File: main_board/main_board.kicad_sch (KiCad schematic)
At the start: 17 parts

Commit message: fix(main_board): fix footprint
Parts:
- added R9: R, Resistor_SMD:R_0603_1608Metric_Pad0.98x0.95mm_HandSolder, symbol Device:R
- C1, C4: footprint (none) -> Capacitor_SMD:C_0603_1608Metric_Pad1.08x0.95mm_HandSolder
- C2, C3: footprint (none) -> Capacitor_SMD:C_0805_2012Metric_Pad1.18x1.45mm_HandSolder
- J1, J2: renamed from J?; footprint (none) -> Connector_Wuerth:Wuerth_WR-WTB_64800311622_1x03_P1.50mm_Vertical
- JSL1: footprint (none) -> Connector_PinHeader_2.00mm:PinHeader_1x08_P2.00mm_Vertical
- R1, R2, R3, R4, R5, R6, R7, R8: footprint (none) -> Resistor_SMD:R_0603_1608Metric_Pad0.98x0.95mm_HandSolder
- gave numbers to parts that had none: 2
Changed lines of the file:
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@@
 (kicad_sch (version 20230121) (generator eeschema)
   (paper "A4")
+  (symbol (lib_id "Device:R") (at 160.02 45.72 0) (unit 1)
+    (in_bom yes) (on_board yes) (dnp no) (fields_autoplaced)
+    (property "Reference" "R9" (at 162.56 44.45 0)
+      (effects (font (size 1.27 1.27)) (justify left))
+    )
+    (property "Value" "R" (at 162.56 46.99 0)
+      (effects (font (size 1.27 1.27)) (justify left))
+    )
+    (property "Footprint" "Resistor_SMD:R_0603_1608Metric_Pad0.98x0.95mm_HandSolder" (at 158.242 45.72 90)
+      (effects (font (size 1.27 1.27)) hide)
+    )
+    (property "Datasheet" "~" (at 160.02 45.72 0)
+      (effects (font (size 1.27 1.27)) hide)
+    )
+    (pin "1")
+    (pin "2")
+    (instances
+      (project "main_board"
+        (path "/e3ba9c21-8631-4c7f-8c4a-647134dd6657"
+          (reference "R9") (unit 1)
+        )
+      )
+    )
+  )
   (symbol (lib_id "Connector_Generic:Conn_01x03") (at 39.37 66.04 0) (unit 1)
     (in_bom yes) (on_board yes) (dnp no) (fields_autoplaced)
-    (property "Reference" "J?" (at 41.91 64.77 0)
+    (property "Reference" "J1" (at 41.91 64.77 0)
       (effects (font (size 1.27 1.27)) (justify left))
     )
@@
       (effects (font (size 1.27 1.27)) (justify left))
     )
-    (property "Footprint" "" (at 39.37 66.04 0)
+    (property "Footprint" "Connector_Wuerth:Wuerth_WR-WTB_64800311622_1x03_P1.50mm_Vertical" (at 39.37 66.04 0)
       (effects (font (size 1.27 1.27)) hide)
     )
@@
       (project "main_board"
         (path "/e3ba9c21-8631-4c7f-8c4a-647134dd6657"
-          (reference "J?") (unit 1)
+          (reference "J1") (unit 1)
         )
       )
@@
       (effects (font (size 1.27 1.27)) (justify left))
     )
-    (property "Footprint" "" (at 109.982 45.72 90)
+    (property "Footprint" "Resistor_SMD:R_0603_1608Metric_Pad0.98x0.95mm_HandSolder" (at 109.982 45.72 90)
       (effects (font (size 1.27 1.27)) hide)
     )
@@
       (effects (font (size 1.27 1.27)) (justify left))
     )
-    (property "Footprint" "" (at 92.202 45.72 90)
+    (property "Footprint" "Resistor_SMD:R_0603_1608Metric_Pad0.98x0.95mm_HandSolder" (at 92.202 45.72 90)
       (effects (font (size 1.27 1.27)) hide)
     )
@@
   (symbol (lib_id "Regulator_Linear:AP130-15Y") (at 173.99 106.68 0) (unit 1)
     (in_bom yes) (on_board yes) (dnp no) (fields_autoplaced)
-    (property "Reference" "U?" (at 173.99 100.33 0)
+    (property "Reference" "U2" (at 173.99 100.33 0)
       (effects (font (size 1.27 1.27)))
     )
@@
       (project "main_board"
         (path "/e3ba9c21-8631-4c7f-8c4a-647134dd6657"
-          (reference "U?") (unit 1)
+          (reference "U2") (unit 1)
         )
       )
@@
   (symbol (lib_id "Connector_Generic:Conn_01x03") (at 63.5 66.04 0) (unit 1)
     (in_bom yes) (on_board yes) (dnp no) (fields_autoplaced)
-    (property "Reference" "J?" (at 66.04 64.77 0)
+    (property "Reference" "J2" (at 66.04 64.77 0)
       (effects (font (size 1.27 1.27)) (justify left))
     )
@@
       (effects (font (size 1.27 1.27)) (justify left))
     )
-    (property "Footprint" "" (at 63.5 66.04 0)
+    (property "Footprint" "Connector_Wuerth:Wuerth_WR-WTB_64800311622_1x03_P1.50mm_Vertical" (at 63.5 66.04 0)
       (effects (font (size 1.27 1.27)) hide)
     )
@@
       (project "main_board"
         (path "/e3ba9c21-8631-4c7f-8c4a-647134dd6657"
-          (reference "J?") (unit 1)
+          (reference "J2") (unit 1)
         )
       )
@@
       (effects (font (size 1.27 1.27)) (justify left))
     )
-    (property "Footprint" "" (at 110.1852 34.29 0)
+    (property "Footprint" "Capacitor_SMD:C_0805_2012Metric_Pad1.18x1.45mm_HandSolder" (at 110.1852 34.29 0)
       (effects (font (size 1.27 1.27)) hide)
     )
@@
       (effects (font (size 1.27 1.27)) (justify left))
     )
-    (property "Footprint" "" (at 141.732 45.72 90)
+    (property "Footprint" "Resistor_SMD:R_0603_1608Metric_Pad0.98x0.95mm_HandSolder" (at 141.732 45.72 90)
       (effects (font (size 1.27 1.27)) hide)
     )
@@
       (effects (font (size 1.27 1.27)) (justify left))
     )
-    (property "Footprint" "" (at 130.5052 34.29 0)
+    (property "Footprint" "Capacitor_SMD:C_0603_1608Metric_Pad1.08x0.95mm_HandSolder" (at 130.5052 34.29 0)
       (effects (font (size 1.27 1.27)) hide)
     )
@@
       (effects (font (size 1.27 1.27)) (justify left))
     )
-    (property "Footprint" "" (at 117.602 45.72 90)
+    (property "Footprint" "Resistor_SMD:R_0603_1608Metric_Pad0.98x0.95mm_HandSolder" (at 117.602 45.72 90)
       (effects (font (size 1.27 1.27)) hide)
     )
@@
       (effects (font (size 1.27 1.27)) (justify left))
     )
-    (property "Footprint" "" (at 125.222 45.72 90)
+    (property "Footprint" "Resistor_SMD:R_0603_1608Metric_Pad0.98x0.95mm_HandSolder" (at 125.222 45.72 90)
       (effects (font (size 1.27 1.27)) hide)
     )
@@
       (effects (font (size 1.27 1.27)) (justify left))
     )
-    (property "Footprint" "" (at 132.842 45.72 90)
+    (property "Footprint" "Resistor_SMD:R_0603_1608Metric_Pad0.98x0.95mm_HandSolder" (at 132.842 45.72 90)
       (effects (font (size 1.27 1.27)) hide)
     )
@@
       (effects (font (size 1.27 1.27)) (justify left))
     )
-    (property "Footprint" "" (at 100.0252 34.29 0)
+    (property "Footprint" "Capacitor_SMD:C_0603_1608Metric_Pad1.08x0.95mm_HandSolder" (at 100.0252 34.29 0)
       (effects (font (size 1.27 1.27)) hide)
     )
@@
       (effects (font (size 1.27 1.27)) (justify left))
     )
-    (property "Footprint" "" (at 120.3452 34.29 0)
+    (property "Footprint" "Capacitor_SMD:C_0805_2012Metric_Pad1.18x1.45mm_HandSolder" (at 120.3452 34.29 0)
       (effects (font (size 1.27 1.27)) hide)
     )
@@
       (effects (font (size 1.27 1.27)) (justify left))
     )
-    (property "Footprint" "" (at 149.352 45.72 90)
+    (property "Footprint" "Resistor_SMD:R_0603_1608Metric_Pad0.98x0.95mm_HandSolder" (at 149.352 45.72 90)
       (effects (font (size 1.27 1.27)) hide)
     )
@@
       (effects (font (size 1.27 1.27)) (justify left))
     )
-    (property "Footprint" "" (at 38.1 38.1 0)
+    (property "Footprint" "Connector_PinHeader_2.00mm:PinHeader_1x08_P2.00mm_Vertical" (at 38.1 38.1 0)
       (effects (font (size 1.27 1.27)) hide)
     )
@@
       (effects (font (size 1.27 1.27)) (justify left))
     )
-    (property "Footprint" "" (at 101.092 45.72 90)
+    (property "Footprint" "Resistor_SMD:R_0603_1608Metric_Pad0.98x0.95mm_HandSolder" (at 101.092 45.72 90)
       (effects (font (size 1.27 1.27)) hide)
     )
@@
   (symbol (lib_id "MCU_STC:STC15W201S-35x-SOP16") (at 104.14 115.57 0) (unit 1)
     (in_bom yes) (on_board yes) (dnp no) (fields_autoplaced)
-    (property "Reference" "U?" (at 106.3341 92.71 0)
+    (property "Reference" "U1" (at 106.3341 92.71 0)
       (effects (font (size 1.27 1.27)) (justify left))
     )
@@
       (project "main_board"
         (path "/e3ba9c21-8631-4c7f-8c4a-647134dd6657"
-          (reference "U?") (unit 1)
-        )
-      )
+          (reference "U1") (unit 1)
+        )
+      )

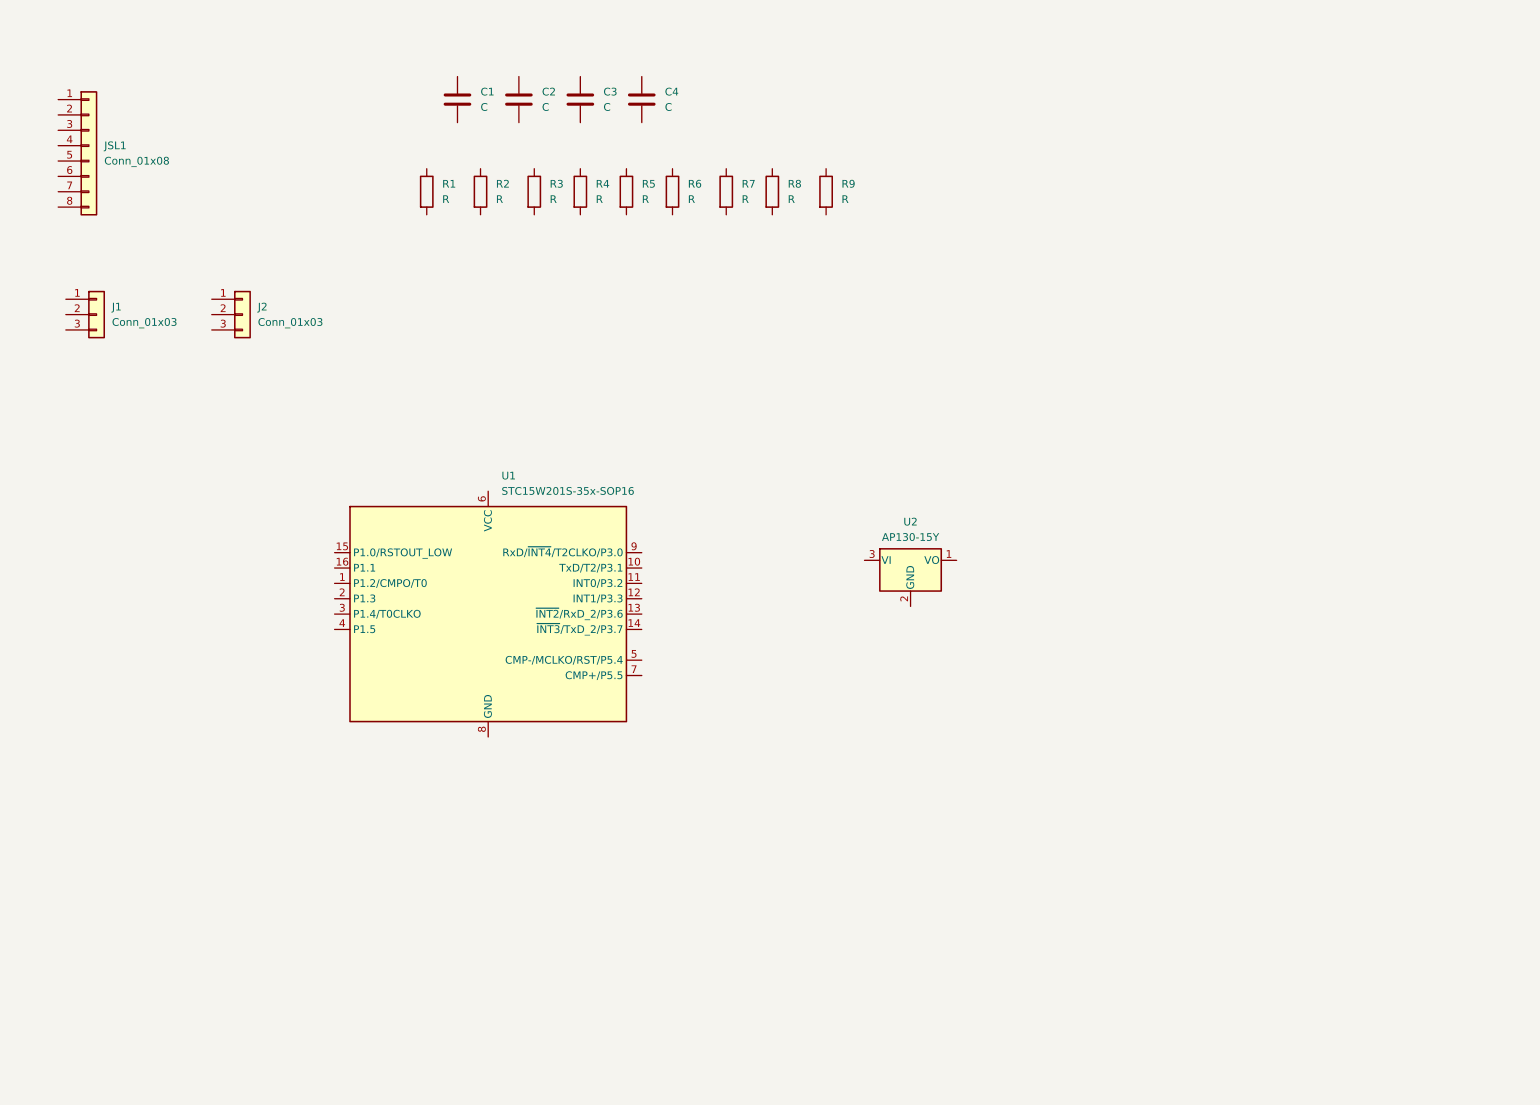
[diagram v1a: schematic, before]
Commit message: feat(main_board): connect net
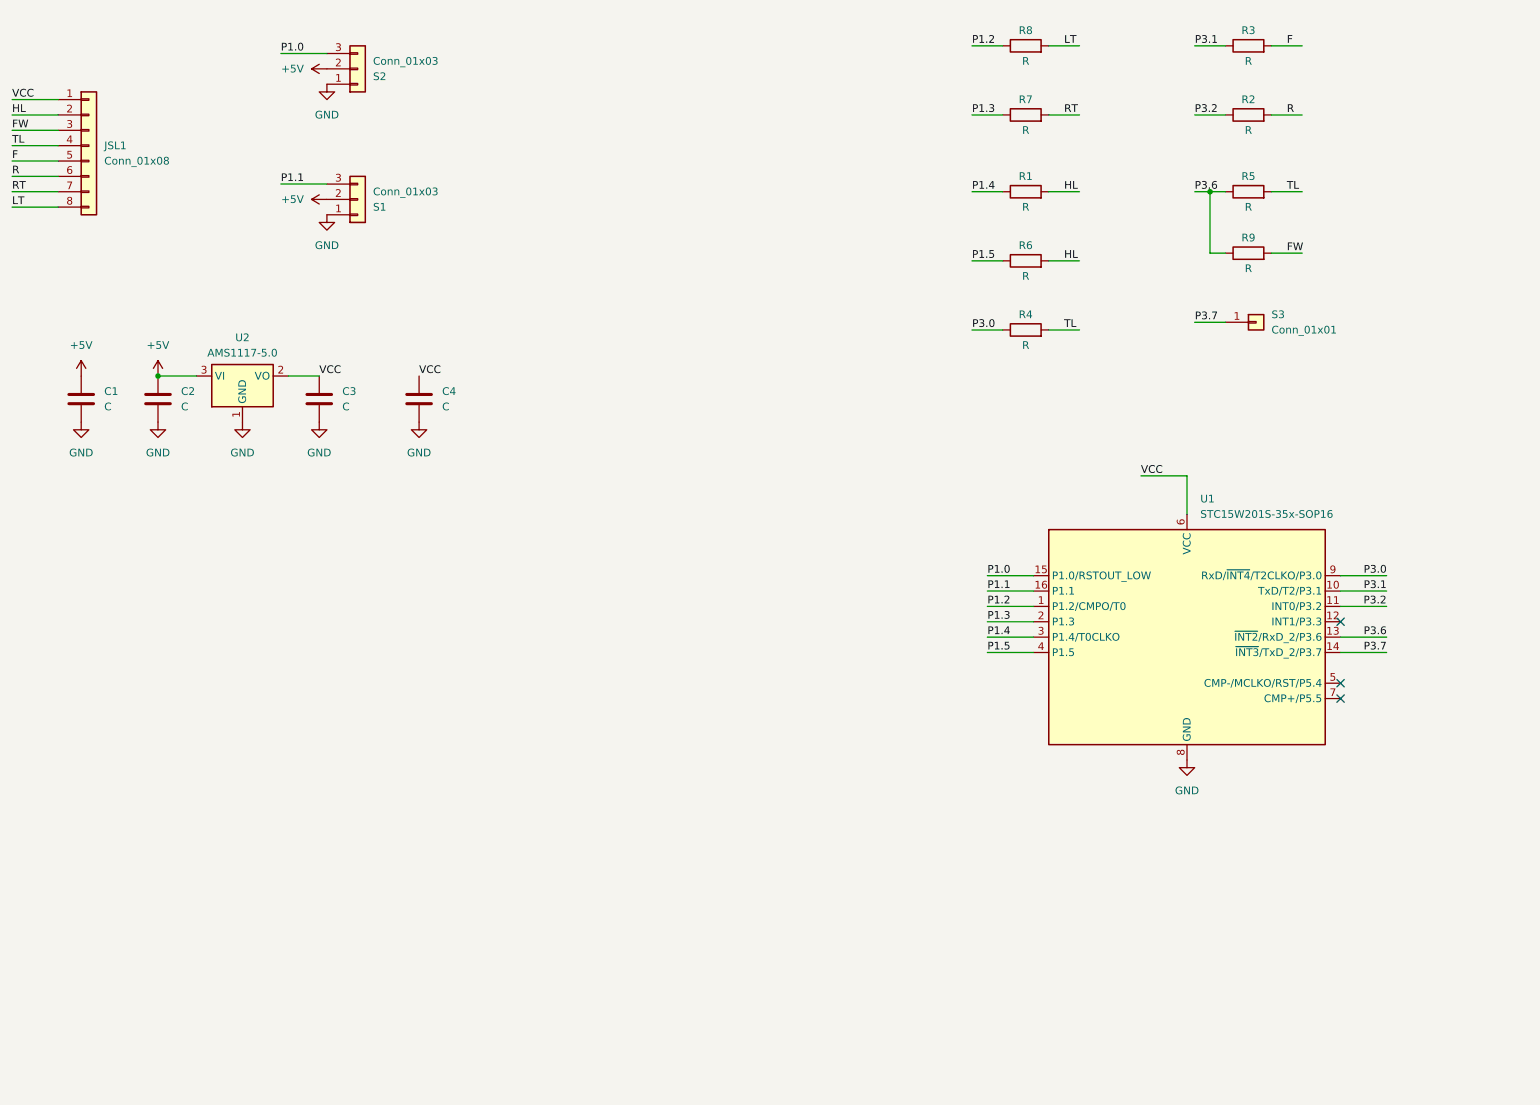
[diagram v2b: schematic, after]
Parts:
- removed U2: AP130-15Y, Package_TO_SOT_SMD:SOT-89-3, symbol Regulator_Linear:AP130-15Y
- added S3: Conn_01x01, TestPoint:TestPoint_THTPad_D1.5mm_Drill0.7mm, symbol Connector_Generic:Conn_01x01
- added U2: AMS1117-5.0, Package_TO_SOT_SMD:SOT-89-3_Handsoldering, symbol Regulator_Linear:AMS1117-5.0
- renumbered J2 to S1, J1 to S2
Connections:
- net P3.6: now reaches R9.1
- net P3.6: now also R5.1, U1.13 (~{INT2}/RxD_2/P3.6)
- net FW: now reaches R9.2
- net FW: now also JSL1.3 (Pin_3)
- net GND: now reaches S2.1 (Pin_1)
- net GND: now also C1.2, C2.2, C3.2, C4.2, S1.1 (Pin_1), U1.8 (GND), U2.1 (GND)
- net +5V: now reaches S2.2 (Pin_2)
- net +5V: now also C1.1, C2.1, S1.2 (Pin_2), U2.3 (VI)
- net P1.0: now reaches S2.3 (Pin_3)
- net P1.0: now also U1.15 (P1.0/RSTOUT_LOW)
- net P3.1: now reaches R3.1
- net P3.1: now also U1.10 (TxD/T2/P3.1)
- net F: now reaches R3.2
- net F: now also JSL1.5 (Pin_5)
- net P1.4: now reaches R1.1
- net P1.4: now also U1.3 (P1.4/T0CLKO)
- net HL: now reaches R1.2
- net HL: now also JSL1.2 (Pin_2), R6.2
- net P1.1: now reaches S1.3 (Pin_3)
- net P1.1: now also U1.16 (P1.1)
- net P1.3: now reaches R7.1
- net P1.3: now also U1.2 (P1.3)
- net RT: now reaches R7.2
- net RT: now also JSL1.7 (Pin_7)
- net VCC: now reaches C4.1
- net VCC: now also C3.1, JSL1.1 (Pin_1), U1.6 (VCC), U2.2 (VO)
- net P3.0: now reaches R4.1
- net P3.0: now also U1.9 (RxD/~{INT4}/T2CLKO/P3.0)
- net TL: now reaches R4.2
- net TL: now also JSL1.4 (Pin_4), R5.2
- net P1.5: now reaches R6.1
- net P1.5: now also U1.4 (P1.5)
- net P1.2: now reaches R8.1
- net P1.2: now also U1.1 (P1.2/CMPO/T0)
- net LT: now reaches R8.2
- net LT: now also JSL1.8 (Pin_8)
- net R: now reaches JSL1.6 (Pin_6)
- net R: now also R2.2
- net P3.2: now reaches R2.1
- net P3.2: now also U1.11 (INT0/P3.2)
- net P3.7: now reaches U1.14 (~{INT3}/TxD_2/P3.7)
- net P3.7: now also S3.1 (Pin_1)
- no-connect marks 0 -> 3
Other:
- moved on the sheet: C1, C2, C3, C4, R1, R2, R3, R4, R5, R6, R7, R8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

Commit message: feat(board/mcu): change mcu to sn32f805
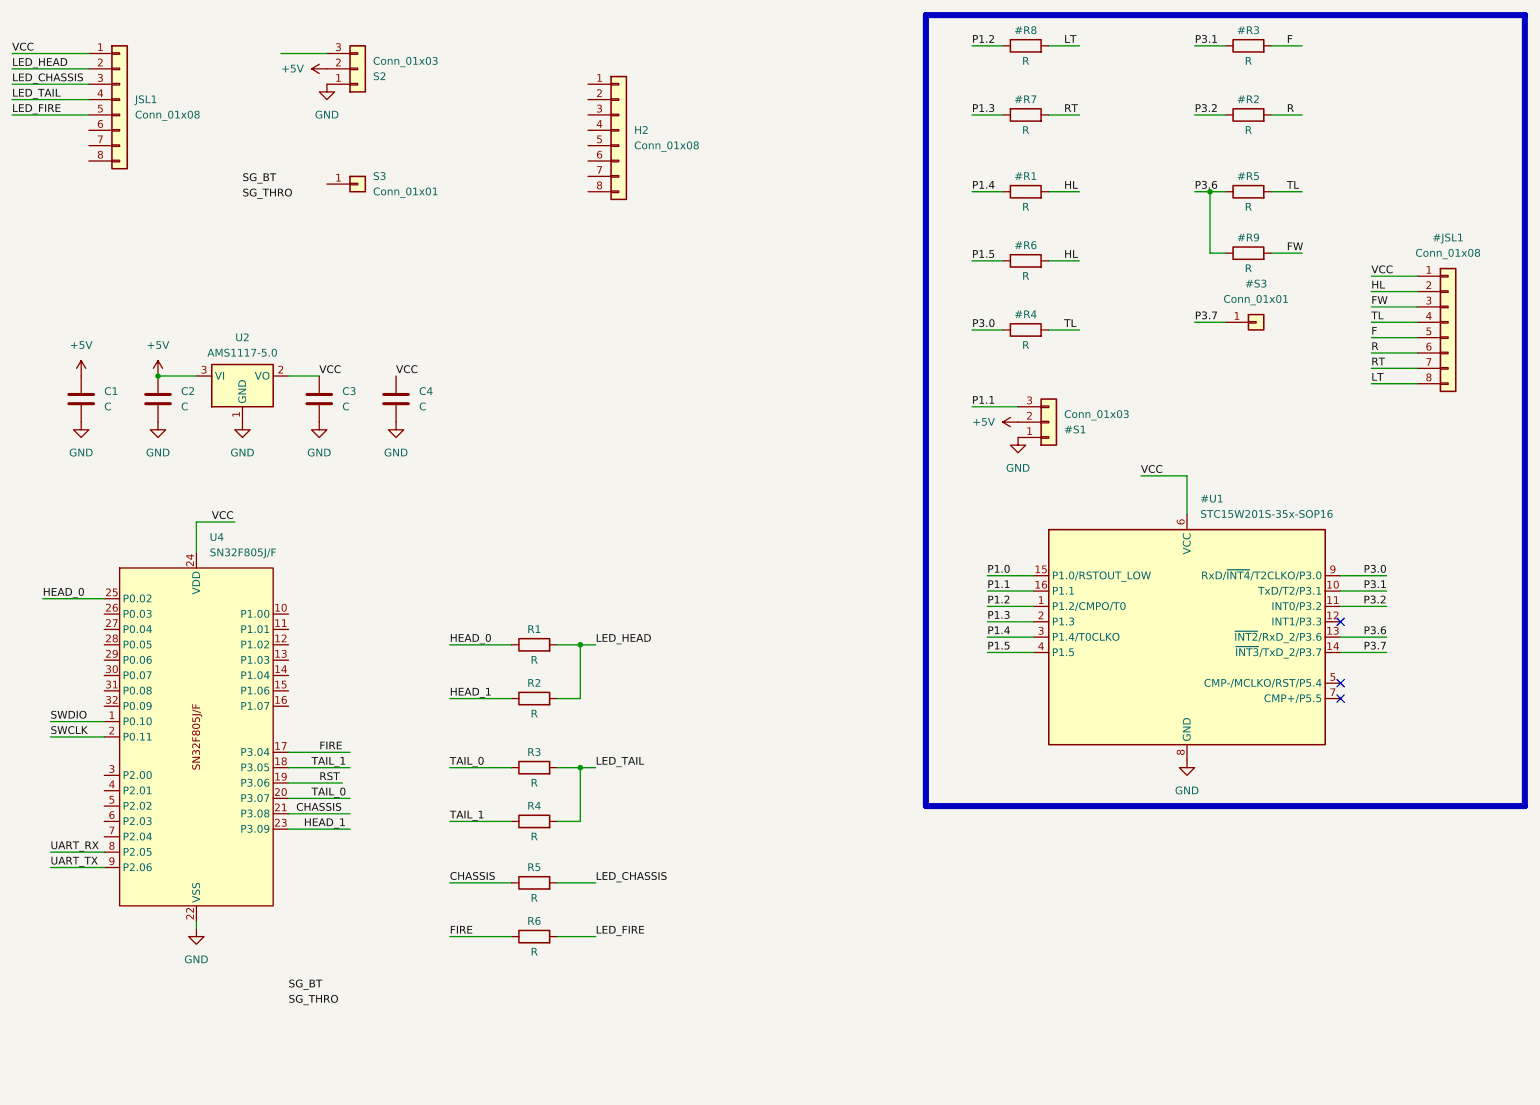
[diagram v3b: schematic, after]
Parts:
- added H2: Conn_01x08, Connector_FFC-FPC:TE_0-1734839-8_1x08-1MP_P0.5mm_Horizontal, symbol Connector_Generic:Conn_01x08
- added JSL1: Conn_01x08, Connector_PinHeader_2.00mm:PinHeader_1x08_P2.00mm_Vertical, symbol Connector_Generic:Conn_01x08
- added R1, R2, R3, R4, R5, R6: R, Resistor_SMD:R_0402_1005Metric, symbol Device:R
- added U4: SN32F805J/F, Package_DFN_QFN:QFN-32-1EP_4x4mm_P0.4mm_EP2.9x2.9mm, symbol SN32F:SN32F800
- C1, C4: footprint Capacitor_SMD:C_0603_1608Metric_Pad1.08x0.95mm_HandSolder -> Capacitor_SMD:C_0402_1005Metric
- U2: footprint Package_TO_SOT_SMD:SOT-89-3_Handsoldering -> Package_TO_SOT_SMD:SOT-89-3
- renumbered JSL1 to #JSL1, R1 to #R1, R2 to #R2, R3 to #R3, R4 to #R4, R5 to #R5, R6 to #R6, R7 to #R7, R8 to #R8, R9 to #R9, S1 to #S1, U1 to #U1
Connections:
- net GND: now also U4.22 (VSS)
- net P1.0: no longer S2.3 (Pin_3)
- net P3.7: no longer S3.1 (Pin_1)
- net VCC: now also JSL1.1 (Pin_1), U4.24 (VDD)
- new net CHASSIS: R5.1, U4.21 (P3.08)
- new net FIRE: R6.1, U4.17 (P3.04)
- new net HEAD_0: R1.1, U4.25 (P0.02)
- new net HEAD_1: R2.1, U4.23 (P3.09)
- new net LED_CHASSIS: JSL1.3 (Pin_3), R5.2
- new net LED_FIRE: JSL1.5 (Pin_5), R6.2
- new net LED_HEAD: JSL1.2 (Pin_2), R1.2, R2.2
- new net LED_TAIL: JSL1.4 (Pin_4), R3.2, R4.2
- new net RST: U4.19 (P3.06)
- new net SWCLK: U4.2 (P0.11)
- new net SWDIO: U4.1 (P0.10)
- new net TAIL_0: R3.1, U4.20 (P3.07)
- new net TAIL_1: R4.1, U4.18 (P3.05)
- new net UART_RX: U4.8 (P2.05)
- new net UART_TX: U4.9 (P2.06)
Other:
- moved on the sheet: C4
